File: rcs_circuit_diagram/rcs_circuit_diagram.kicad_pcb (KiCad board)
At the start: 2 copper layers, 49 parts, among them J1 Conn_01x06_Pin, J11 Conn_01x02_Pin, J13 Conn_01x02_Pin, J15 Conn_01x02_Pin, J3 Conn_01x02_Pin, J6 Conn_01x02_Pin, J7 Conn_01x02_Pin, J9 Conn_01x02_Pin, U1 LM2596S-5

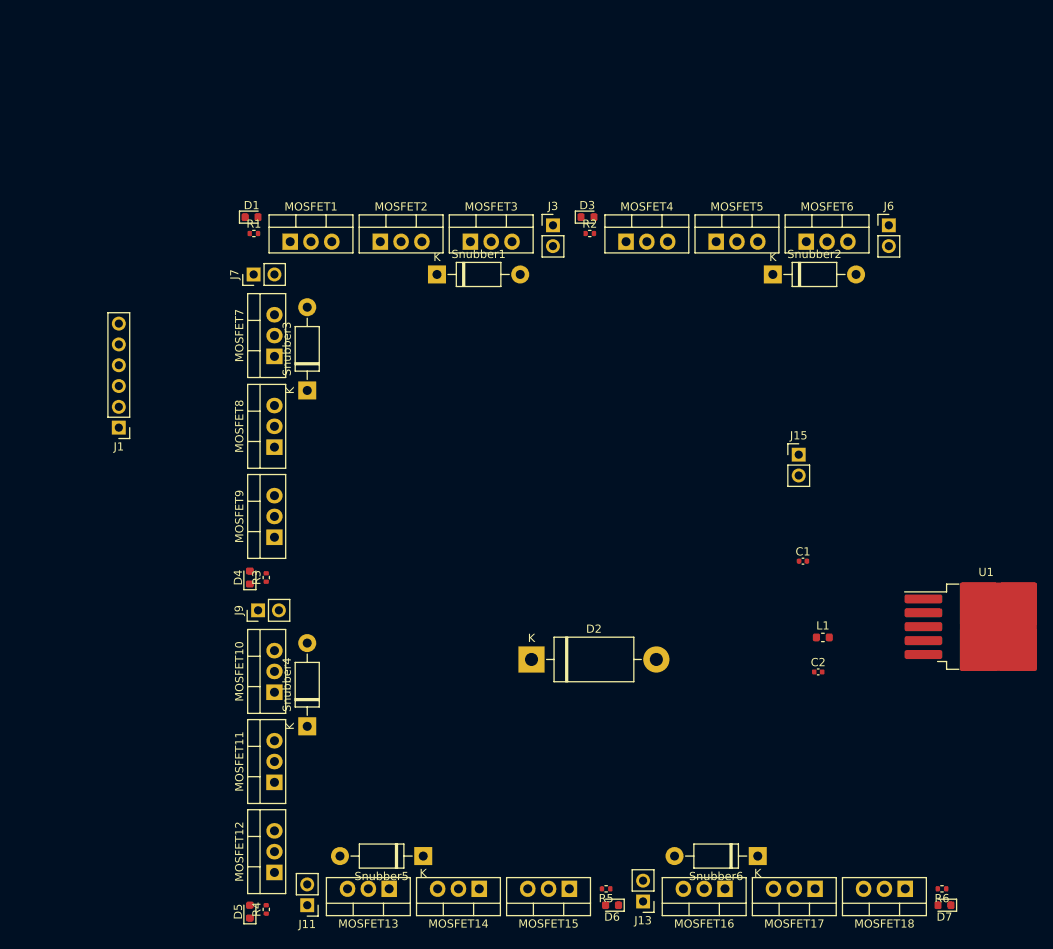
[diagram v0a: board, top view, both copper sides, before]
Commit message: Rearranged components
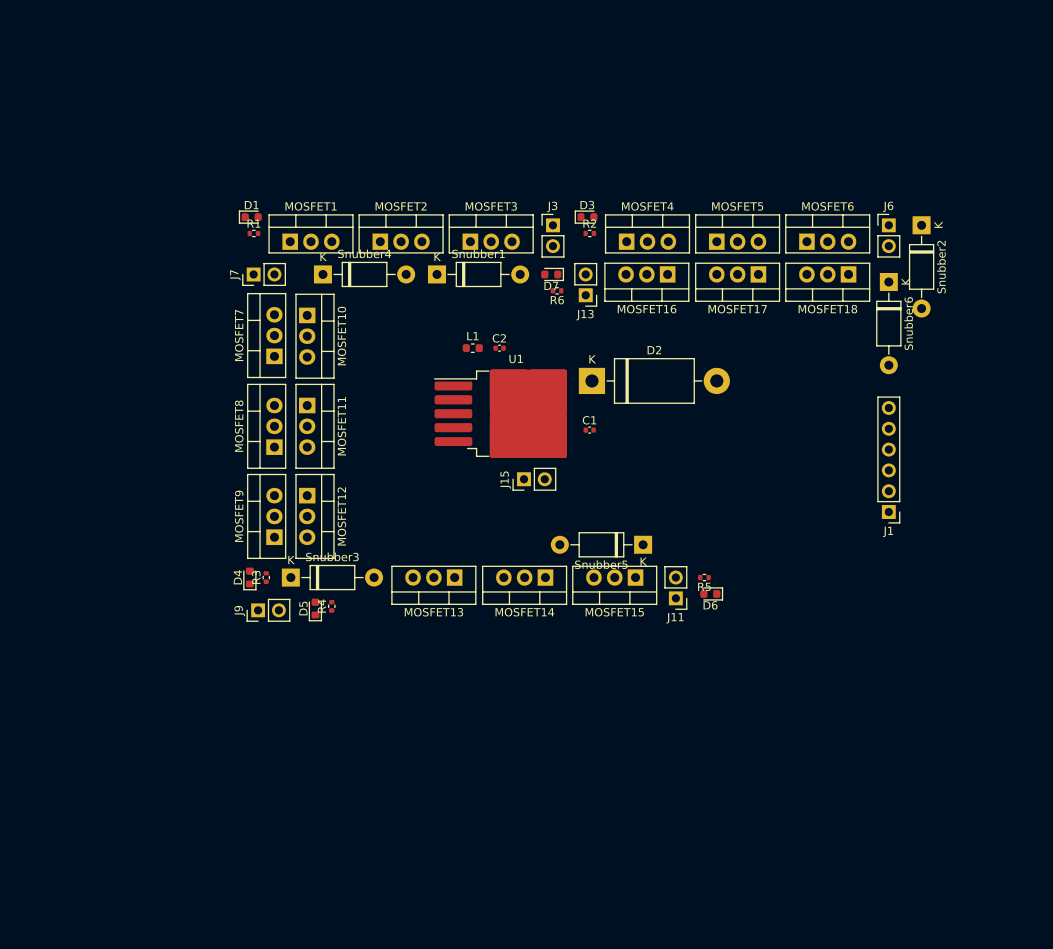
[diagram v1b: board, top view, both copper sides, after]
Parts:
- moved J1 94.6 mm to (176.0, 93.0)
- moved D7 90.7 mm to (134.8, 64.0)
- moved R6 86.8 mm to (135.5, 66.0)
- moved MOSFET16 75.3 mm to (149.0, 64.0)
- moved MOSFET17 75.3 mm to (160.1, 64.0)
- moved MOSFET18 75.3 mm to (171.1, 64.0)
- moved J13 74.3 mm to (139.0, 66.5)
- moved Snubber6 71.9 mm to (176.0, 64.9), turned to -90 degrees
- moved U1 63.0 mm to (130.5, 81.0)
- moved J11 58.6 mm to (150.0, 103.5)
- moved C2 55.5 mm to (128.5, 73.0)
- moved L1 55.4 mm to (125.2, 73.0)
- moved Snubber4 55.2 mm to (106.9, 64.0), turned to 0 degrees
- moved Snubber5 46.5 mm to (146.0, 97.0)
- moved MOSFET10 46.2 mm to (105.0, 69.0), turned to -90 degrees
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
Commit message: Updated footprints, changed layout of components
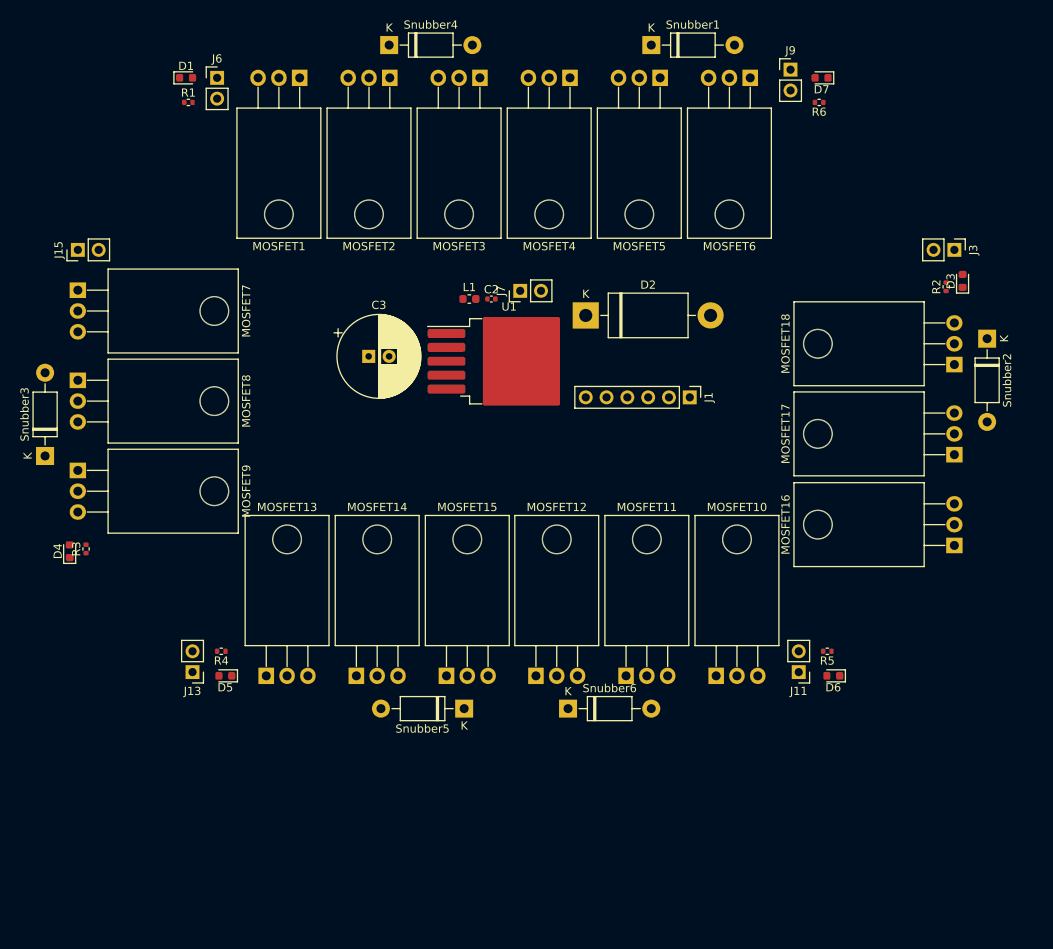
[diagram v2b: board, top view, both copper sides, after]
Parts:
- removed C1: 680 uF, Capacitor_SMD:C_0402_1005Metric
- added C3: C_Polarized, Capacitor_THT:CP_Radial_D10.0mm_P2.50mm, F.Cu at (112.5, 74.0)
- MOSFET1, MOSFET10, MOSFET11, MOSFET12, MOSFET13, MOSFET14, MOSFET15, MOSFET16, MOSFET17, MOSFET18, MOSFET2, MOSFET3, MOSFET4, MOSFET5, MOSFET6, MOSFET7, MOSFET8, MOSFET9: footprint Package_TO_SOT_THT:TO-220-3_Vertical -> Package_TO_SOT_THT:TO-220-3_Horizontal_TabDown
- moved J9 92.6 mm to (164.0, 39.0), turned to 0 degrees
- moved J6 84.0 mm to (94.0, 40.0)
- moved MOSFET10 66.5 mm to (154.9, 113.0), turned to 0 degrees
- moved J13 66.5 mm to (91.0, 112.5)
- moved Snubber6 65.2 mm to (136.8, 117.0), turned to 0 degrees
- moved J15 61.2 mm to (77.0, 61.0)
- moved MOSFET11 51.0 mm to (143.9, 113.0), turned to 0 degrees
- moved J3 49.1 mm to (184.0, 61.0), turned to -90 degrees
- moved MOSFET16 48.2 mm to (184.0, 97.1), turned to 90 degrees
- moved D3 46.4 mm to (185.0, 64.8), turned to 90 degrees
- moved R2 44.0 mm to (183.0, 65.5), turned to 90 degrees
- moved D7 40.8 mm to (167.8, 40.0)
- moved R6 39.4 mm to (167.5, 43.0)
- moved Snubber1 38.3 mm to (147.0, 36.0)
- moved MOSFET12 35.5 mm to (132.9, 113.0), turned to 0 degrees
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
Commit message: Routing
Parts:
- moved J9 70.2 mm to (98.0, 63.0)
- moved J15 59.5 mm to (136.5, 62.0)
- moved J6 54.8 mm to (126.0, 84.5)
- moved R4 54.6 mm to (142.5, 84.0)
- moved D5 53.5 mm to (141.8, 87.0)
- moved MOSFET12 50.8 mm to (182.7, 102.5), turned to 90 degrees
- moved MOSFET9 48.4 mm to (120.5, 109.2), turned to 0 degrees
- moved MOSFET7 48.3 mm to (98.5, 109.2), turned to 0 degrees
- moved D6 46.3 mm to (130.2, 88.0)
- moved MOSFET8 45.8 mm to (109.5, 109.2), turned to 0 degrees
- moved R5 45.5 mm to (130.5, 85.0)
- moved MOSFET11 44.3 mm to (182.7, 91.5), turned to 90 degrees
- moved MOSFET10 43.3 mm to (183.0, 80.1), turned to 90 degrees
- moved Snubber3 40.9 mm to (106.0, 62.0), turned to 0 degrees
- moved J11 37.5 mm to (137.5, 87.0), turned to -90 degrees
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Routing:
- net GND: track 0.00 -> 297.8 mm, vias 0 -> 1
- net VCC: track 0.00 -> 206.9 mm, vias 0 -> 4
- net Net-(D1-K): track 0.00 -> 107.5 mm
- net Net-(D5-K): track 0.00 -> 105.6 mm, vias 0 -> 2
- net Net-(D3-K): track 0.00 -> 101.2 mm, vias 0 -> 3
- net Net-(D7-K): track 0.00 -> 99.6 mm
- net Net-(D4-K): track 0.00 -> 89.7 mm, vias 0 -> 2
- net Net-(D6-K): track 0.00 -> 82.4 mm, vias 0 -> 2
- net Net-(J1-Pin_1): track 0.00 -> 76.2 mm, vias 0 -> 2
- net /sol5: track 0.00 -> 72.9 mm, vias 0 -> 2
- net /sol4: track 0.00 -> 69.4 mm, vias 0 -> 2
- net /sol6: track 0.00 -> 67.7 mm, vias 0 -> 1
- net /sol3: track 0.00 -> 67.6 mm, vias 0 -> 1
- net /sol2: track 0.00 -> 65.8 mm, vias 0 -> 3
- net Net-(D2-K): track 0.00 -> 27.4 mm, vias 0 -> 2
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- added copper zone on B.Cu, net GND
- added copper zone on F.Cu, net GND

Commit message: Everything is very much not right
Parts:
- added J2: Conn_01x02_Pin, Connector_PinHeader_2.54mm:PinHeader_1x02_P2.54mm_Vertical, F.Cu at (101.0, 71.5)
- moved J1 55.2 mm to (97.0, 71.4), turned to 0 degrees
- moved J6 25.8 mm to (101.0, 78.0)
- moved J13 14.4 mm to (112.0, 83.0), turned to -90 degrees
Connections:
- C2 pad 1: VCC -> Net-(J1-Pin_1)
- C2 pad 2: GND -> Net-(J1-Pin_1)
- C3 pad 1: VCC -> Net-(J1-Pin_1)
- C3 pad 2: GND -> Net-(J1-Pin_1)
- D1 pad 1: Net-(D1-K) -> Net-(J1-Pin_1)
- D1 pad 2: Net-(D1-A) -> Net-(J1-Pin_1)
- D2 pad 1: Net-(D2-K) -> Net-(J1-Pin_1)
- D3 pad 1: Net-(D3-K) -> Net-(J1-Pin_1)
- D3 pad 2: Net-(D3-A) -> Net-(J1-Pin_1)
- D4 pad 1: Net-(D4-K) -> Net-(J1-Pin_1)
- D4 pad 2: Net-(D4-A) -> Net-(J1-Pin_1)
- D7 pad 1: Net-(D7-K) -> Net-(J1-Pin_1)
- D7 pad 2: Net-(D7-A) -> Net-(J1-Pin_1)
- J13 pad 2: VCC -> Net-(J1-Pin_1)
- J15 pad 1: Net-(D7-K) -> Net-(J1-Pin_1)
- J15 pad 2: VCC -> Net-(J1-Pin_1)
- J3 pad 1: Net-(D1-K) -> Net-(J1-Pin_1)
- J3 pad 2: VCC -> Net-(J1-Pin_1)
- J6 pad 1: VCC -> Net-(J1-Pin_1)
- J7 pad 1: Net-(D3-K) -> Net-(J1-Pin_1)
- J7 pad 2: VCC -> Net-(J1-Pin_1)
- J9 pad 1: Net-(D4-K) -> Net-(J1-Pin_1)
- J9 pad 2: VCC -> Net-(J1-Pin_1)
- L1 pad 1: Net-(D2-K) -> Net-(J1-Pin_1)
- L1 pad 2: VCC -> Net-(J1-Pin_1)
- MOSFET1 pad 2: Net-(D1-K) -> Net-(J1-Pin_1)
- MOSFET1 pad 3: GND -> Net-(J1-Pin_1)
- MOSFET10 pad 3: GND -> Net-(J1-Pin_1)
- MOSFET11 pad 3: GND -> Net-(J1-Pin_1)
- MOSFET12 pad 3: GND -> Net-(J1-Pin_1)
- MOSFET13 pad 3: GND -> Net-(J1-Pin_1)
- MOSFET14 pad 3: GND -> Net-(J1-Pin_1)
- MOSFET15 pad 3: GND -> Net-(J1-Pin_1)
- MOSFET16 pad 2: Net-(D7-K) -> Net-(J1-Pin_1)
- MOSFET16 pad 3: GND -> Net-(J1-Pin_1)
- MOSFET17 pad 2: Net-(D7-K) -> Net-(J1-Pin_1)
- MOSFET17 pad 3: GND -> Net-(J1-Pin_1)
- MOSFET18 pad 2: Net-(D7-K) -> Net-(J1-Pin_1)
- MOSFET18 pad 3: GND -> Net-(J1-Pin_1)
- MOSFET2 pad 2: Net-(D1-K) -> Net-(J1-Pin_1)
- MOSFET2 pad 3: GND -> Net-(J1-Pin_1)
- MOSFET3 pad 2: Net-(D1-K) -> Net-(J1-Pin_1)
- MOSFET3 pad 3: GND -> Net-(J1-Pin_1)
- MOSFET4 pad 2: Net-(D3-K) -> Net-(J1-Pin_1)
- MOSFET4 pad 3: GND -> Net-(J1-Pin_1)
- MOSFET5 pad 2: Net-(D3-K) -> Net-(J1-Pin_1)
- MOSFET5 pad 3: GND -> Net-(J1-Pin_1)
- MOSFET6 pad 2: Net-(D3-K) -> Net-(J1-Pin_1)
- MOSFET6 pad 3: GND -> Net-(J1-Pin_1)
- MOSFET7 pad 2: Net-(D4-K) -> Net-(J1-Pin_1)
- MOSFET7 pad 3: GND -> Net-(J1-Pin_1)
- MOSFET8 pad 2: Net-(D4-K) -> Net-(J1-Pin_1)
- MOSFET8 pad 3: GND -> Net-(J1-Pin_1)
- MOSFET9 pad 2: Net-(D4-K) -> Net-(J1-Pin_1)
- MOSFET9 pad 3: GND -> Net-(J1-Pin_1)
- R1 pad 1: VCC -> Net-(J1-Pin_1)
- R1 pad 2: Net-(D1-A) -> Net-(J1-Pin_1)
- R2 pad 1: VCC -> Net-(J1-Pin_1)
- R2 pad 2: Net-(D3-A) -> Net-(J1-Pin_1)
- R3 pad 1: VCC -> Net-(J1-Pin_1)
- R3 pad 2: Net-(D4-A) -> Net-(J1-Pin_1)
- R6 pad 1: VCC -> Net-(J1-Pin_1)
- R6 pad 2: Net-(D7-A) -> Net-(J1-Pin_1)
- Snubber1 pad 1: VCC -> Net-(J1-Pin_1)
- Snubber1 pad 2: Net-(D1-K) -> Net-(J1-Pin_1)
- Snubber2 pad 1: VCC -> Net-(J1-Pin_1)
- Snubber2 pad 2: Net-(D3-K) -> Net-(J1-Pin_1)
- Snubber3 pad 1: VCC -> Net-(J1-Pin_1)
- Snubber3 pad 2: Net-(D4-K) -> Net-(J1-Pin_1)
- Snubber4 pad 1: VCC -> Net-(J1-Pin_1)
- Snubber5 pad 1: VCC -> Net-(J1-Pin_1)
- Snubber6 pad 2: Net-(D7-K) -> Net-(J1-Pin_1)
- U1 pad 1: VCC -> Net-(J1-Pin_1)
- U1 pad 2: Net-(D2-K) -> Net-(J1-Pin_1)
- U1 pad 4: VCC -> Net-(J1-Pin_1)
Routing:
- net Net-(J1-Pin_1): track 76.2 -> 982.0 mm, vias 2 -> 10
- net GND: track 297.8 -> 14.7 mm, vias 1 -> 0
- net VCC: track 206.9 -> 18.4 mm, vias 4 -> 1
- net Net-(D1-K): track 107.5 -> 0.00 mm
- net Net-(D3-K): track 101.2 -> 0.00 mm, vias 3 -> 0
- net Net-(D7-K): track 99.6 -> 0.00 mm
- net Net-(D4-K): track 89.7 -> 0.00 mm, vias 2 -> 0
- net /sol4: track 69.4 -> 147.9 mm, vias 2 -> 0
- net /sol5: track 72.9 -> 119.2 mm, vias 2 -> 0
- net /sol2: track 65.8 -> 101.6 mm, vias 3 -> 0
- net Net-(D2-K): track 27.4 -> 0.00 mm, vias 2 -> 0
- net /sol3: track 67.6 -> 59.8 mm, vias 1 -> 0
- net Net-(D6-K): track 82.4 -> 77.1 mm
- net Net-(D7-A): track 3.83 -> 0.00 mm
- net Net-(D1-A): track 3.32 -> 0.00 mm
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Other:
- board outline added: 96 x 78 mm

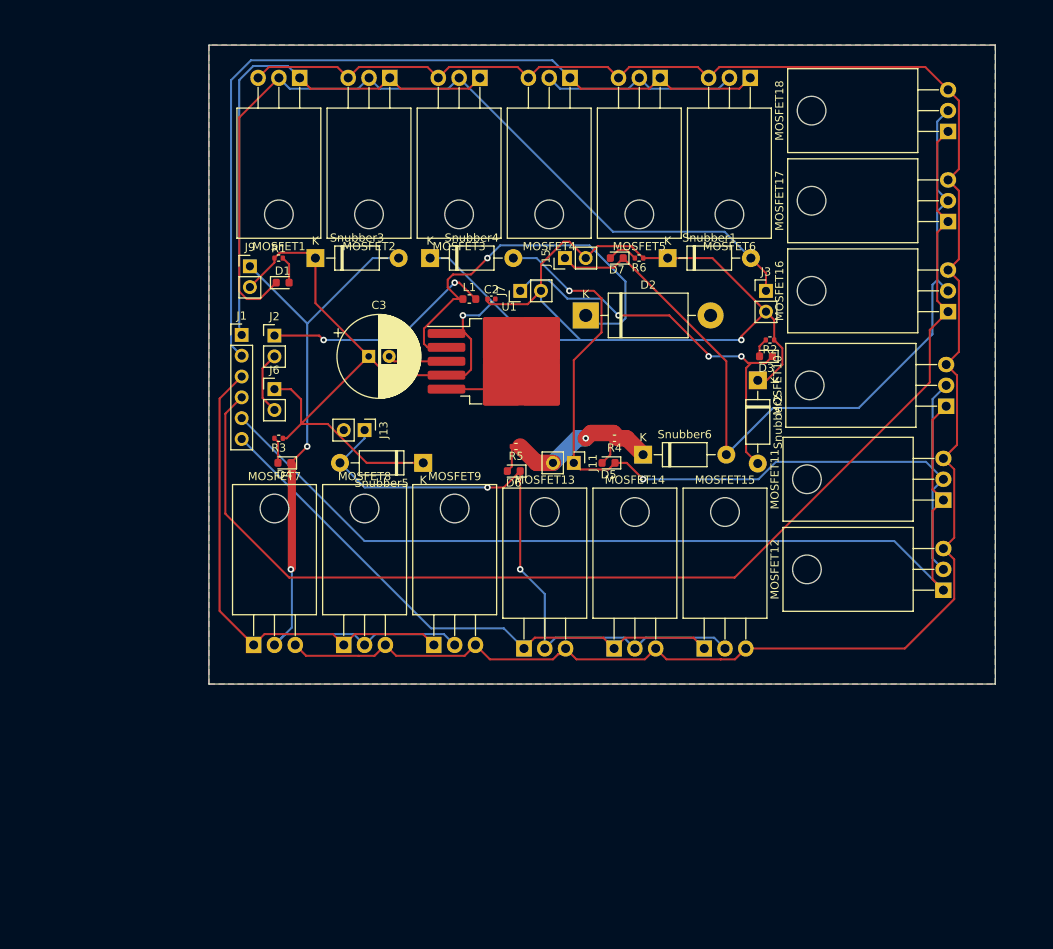
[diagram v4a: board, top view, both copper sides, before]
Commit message: deleted all traces and started routing again
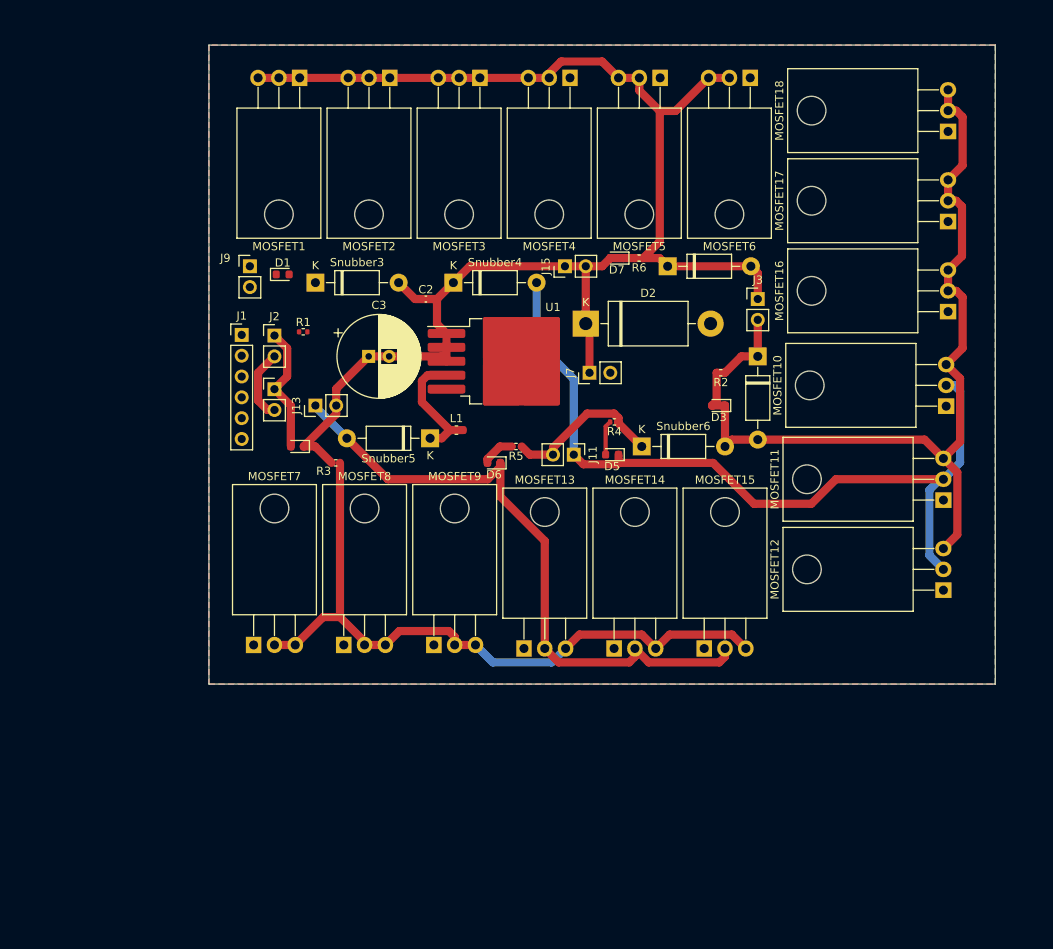
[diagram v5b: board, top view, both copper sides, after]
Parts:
- moved L1 16.1 mm to (123.2, 83.0)
- moved J7 13.1 mm to (139.5, 76.0)
- moved R1 9.49 mm to (104.5, 71.0)
- moved D3 8.34 mm to (155.2, 80.0)
- moved C2 8.00 mm to (119.5, 67.0)
- moved R3 7.60 mm to (108.5, 87.0)
- moved R2 7.21 mm to (155.5, 76.0)
- moved J13 6.71 mm to (106.0, 80.0), turned to 90 degrees
- moved Snubber4 4.13 mm to (122.8, 65.0)
- moved Snubber5 3.12 mm to (120.0, 84.0)
- moved Snubber3 3.00 mm to (106.0, 65.0)
- moved Snubber2 2.92 mm to (160.0, 74.0)
- moved D6 2.62 mm to (127.8, 87.0)
- moved D4 2.55 mm to (103.8, 85.0)
- moved R4 2.00 mm to (142.5, 82.0)
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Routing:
- net Net-(J1-Pin_1): track 982.0 -> 413.6 mm, vias 10 -> 0
- net /sol4: track 147.9 -> 0.00 mm
- net /sol5: track 119.2 -> 0.00 mm
- net /sol2: track 101.6 -> 0.00 mm
- net /sol6: track 69.2 -> 0.00 mm
- net /sol3: track 59.8 -> 0.00 mm
- net Net-(D5-K): track 105.6 -> 99.1 mm, vias 2 -> 0
- net GND: track 14.7 -> 8.69 mm
- net Net-(D6-K): track 77.1 -> 78.4 mm, vias 2 -> 0
- net VCC: track 18.4 -> 19.7 mm, vias 1 -> 0
- net Net-(D6-A): track 3.23 -> 4.09 mm
- net Net-(D5-A): track 3.41 -> 4.23 mm

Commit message: Finished routing, 1mm traces
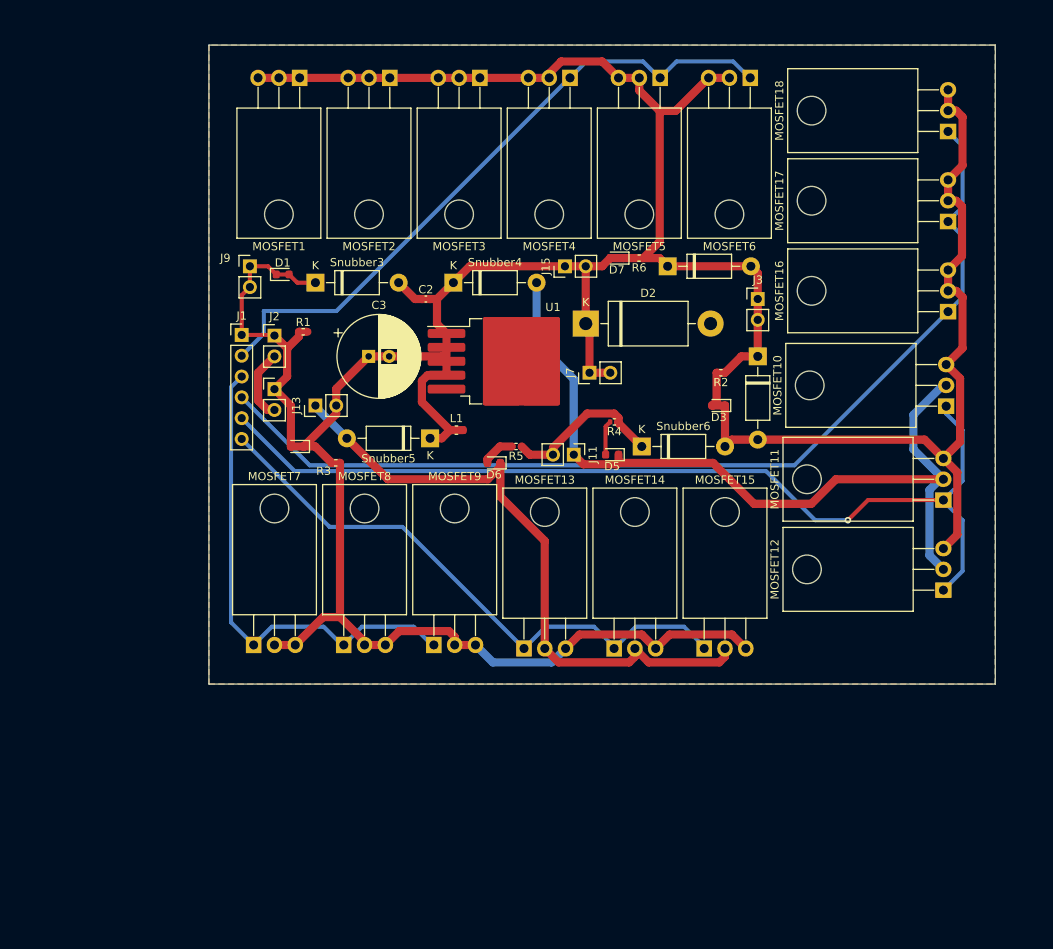
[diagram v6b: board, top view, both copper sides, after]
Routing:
- net /sol4: track 0.00 -> 122.4 mm
- net /sol5: track 0.00 -> 118.0 mm, vias 0 -> 1
- net /sol2: track 0.00 -> 81.1 mm
- net /sol6: track 0.00 -> 71.7 mm
- net /sol3: track 0.00 -> 60.1 mm
- net Net-(J1-Pin_1): track 413.6 -> 448.2 mm
- net Net-(D5-K): track 99.1 -> 100.4 mm
